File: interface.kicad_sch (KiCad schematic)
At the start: 2 parts, among them U1 2.42OLED

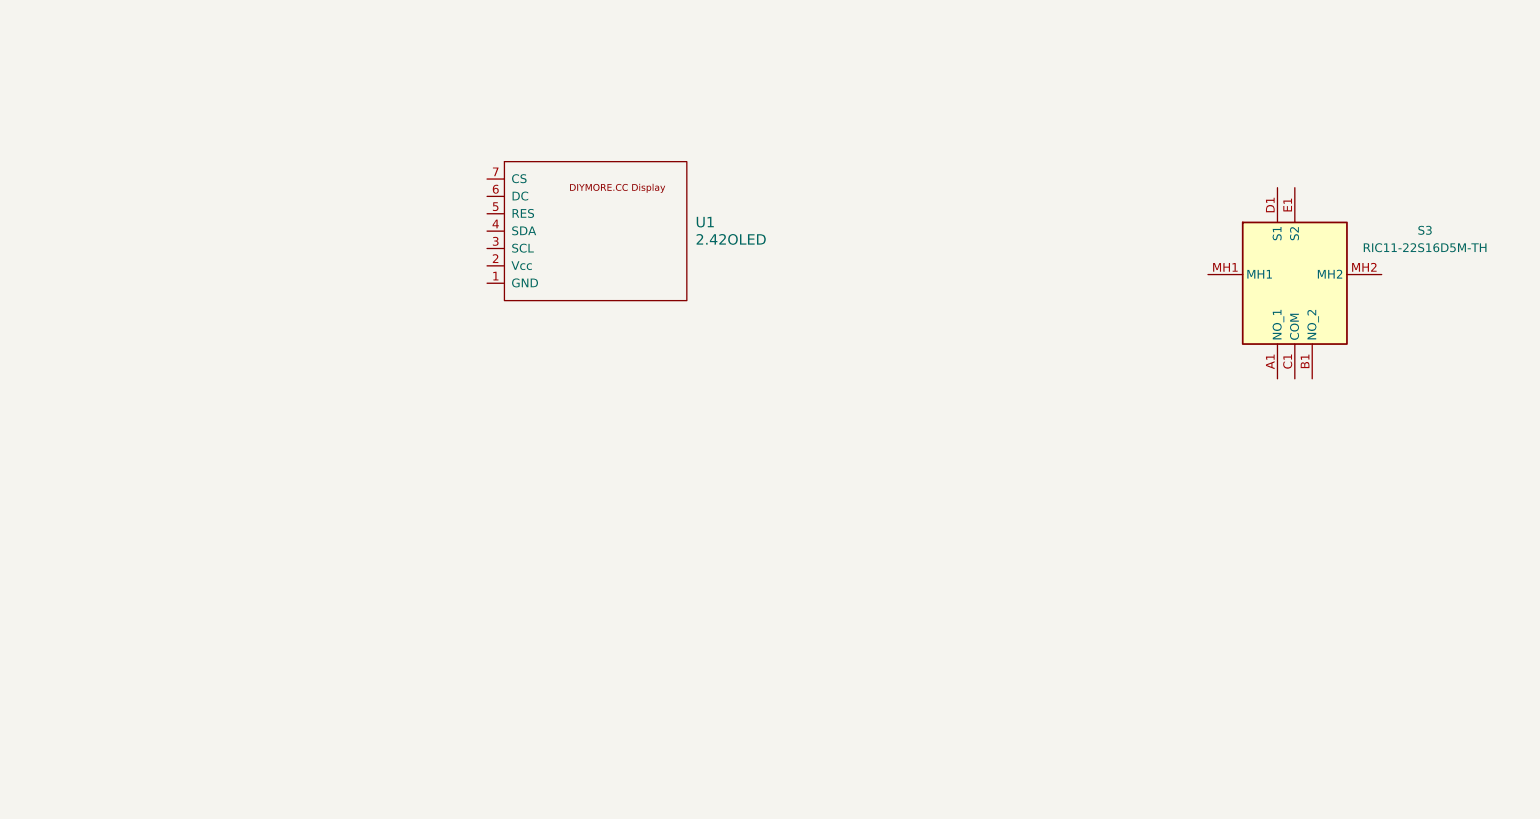
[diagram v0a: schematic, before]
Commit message: improve power delivery schema, improve dac, added oled, encoder, audio out
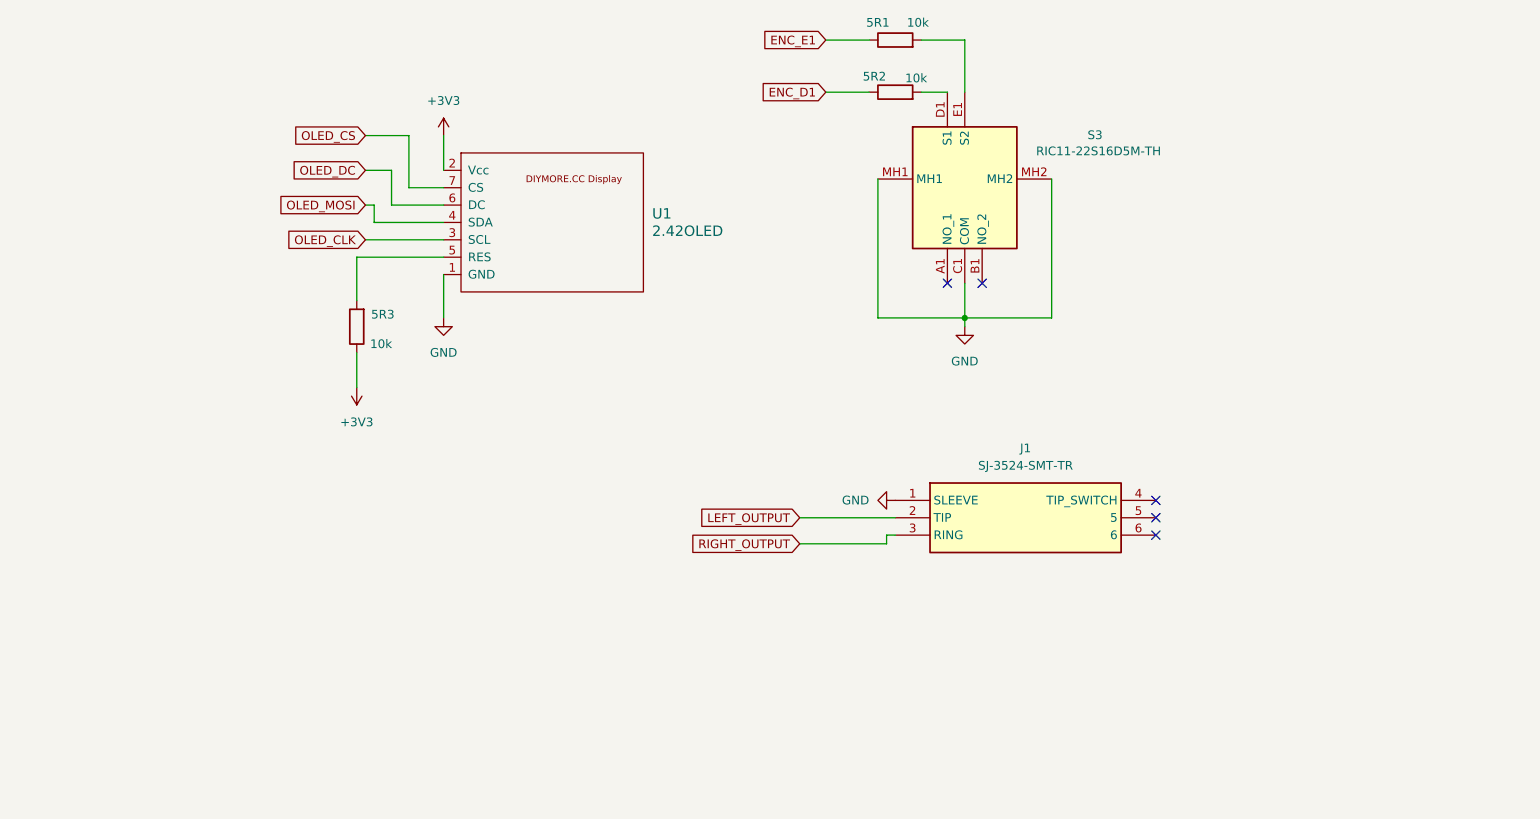
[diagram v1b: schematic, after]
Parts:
- added 5R1, 5R2, 5R3: 10k, symbol Device:R
- added J1: SJ-3524-SMT-TR, ipradio:SJ3524SMTTR, symbol ipradio:SJ-3524-SMT-TR
- S3: footprint RIC1122S16D5MTH -> ipradio:RIC1122S16D5MTH
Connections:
- net GND: now reaches U1.1 (GND)
- net GND: now also S3.C1 (COM), S3.MH1, S3.MH2, J1.1 (SLEEVE)
- net +3V3: now reaches U1.2 (Vcc)
- net +3V3: now also 5R3.1
- net OLED_CLK: now reaches U1.3 (SCL)
- net OLED_MOSI: now reaches U1.4 (SDA)
- net at U1.5 (RES): now also 5R3.2
- net OLED_DC: now reaches U1.6 (DC)
- net OLED_CS: now reaches U1.7 (CS)
- net at S3.D1 (S1): now also 5R2.2
- net at S3.E1 (S2): now also 5R1.2
- new net ENC_D1: 5R2.1
- new net ENC_E1: 5R1.1
- new net LEFT_OUTPUT: J1.2 (TIP)
- new net RIGHT_OUTPUT: J1.3 (RING)
- no-connect marks 0 -> 5
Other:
- moved on the sheet: S3, U1

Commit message: finalize power and esp schemas
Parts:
- 5R1, 5R2, 5R3: footprint (none) -> Resistor_SMD:R_0402_1005Metric
- U1: footprint (none) -> ipradio:DIYMORE.CC
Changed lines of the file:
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@@
 	(paper "A4")
+	(junction
+		(at 100.33 62.23)
+		(diameter 0)
+		(color 0 0 0 0)
+	)
 	(junction
 		(at 176.53 88.9)
@@
 			)
 		)
-		(property "Footprint" ""
+		(property "Footprint" "Resistor_SMD:R_0402_1005Metric"
 			(at 166.37 57.658 90)
 			(hide yes)
@@
 			)
 		)
-		(property "Footprint" ""
+		(property "Footprint" "Resistor_SMD:R_0402_1005Metric"
 			(at 166.37 50.038 90)
 			(hide yes)
@@
 			)
 		)
-		(property "Footprint" ""
+		(property "Footprint" "ipradio:DIYMORE.CC"
 			(at 102.87 86.36 0)
 			(hide yes)
@@
 			)
 		)
-		(property "Footprint" ""
+		(property "Footprint" "Resistor_SMD:R_0402_1005Metric"
 			(at 89.408 90.17 90)
 			(hide yes)
@@
 					(unit 1)
 				)
+			)
+		)
+	)
+	(symbol
+		(lib_id "power:PWR_FLAG")
+		(at 100.33 62.23 270)
+		(unit 1)
+		(body_style 1)
+		(exclude_from_sim no)
+		(in_bom yes)
+		(on_board yes)
+		(in_pos_files yes)
+		(dnp no)
+		(fields_autoplaced yes)
+		(property "Reference" "#FLG01"
+			(at 102.235 62.23 0)
+			(hide yes)
+			(show_name no)
+			(do_not_autoplace no)
+			(effects
+				(font
+					(size 1.27 1.27)
+				)
+			)
+		)
+		(property "Value" "PWR_FLAG"
+			(at 104.14 62.2299 90)
+			(show_name no)
+			(do_not_autoplace no)
+			(effects
+				(font
+					(size 1.27 1.27)
+				)
+				(justify left)
+			)
+		)
+		(property "Footprint" ""
+			(at 100.33 62.23 0)
+			(hide yes)
+			(show_name no)
+			(do_not_autoplace no)
+			(effects
+				(font
+					(size 1.27 1.27)
+				)
+			)
+		)
+		(property "Datasheet" ""
+			(at 100.33 62.23 0)
+			(hide yes)
+			(show_name no)
+			(do_not_autoplace no)
+			(effects
+				(font
+					(size 1.27 1.27)
+				)
+			)
+		)
+		(property "Description" "Special symbol for telling ERC where power comes from"
+			(at 100.33 62.23 0)
+			(hide yes)
+			(show_name no)
+			(do_not_autoplace no)
+			(effects
+				(font
+					(size 1.27 1.27)
+				)
+			)
+		)
+		(pin "1"
+		)
+		(instances
+			(project "ipradio"
+				(path "/8a54d64b-fc0c-416f-bc23-c8cdbd245f9f/68655846-d262-4627-826b-c40a0dd3f1c4"
+					(reference "#FLG01")
+					(unit 1)
+				)

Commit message: finalized schema
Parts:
- added 5C3, 5C4, 5C7: 100nF, Capacitor_SMD:C_0402_1005Metric, symbol Device:C
- added 5C5: 1uF, Capacitor_SMD:C_0402_1005Metric, symbol Device:C
- added 5C6: 10uF, Capacitor_SMD:C_0402_1005Metric, symbol Device:C
- added R2, R3, R4: 5.1k, Resistor_SMD:R_0402_1005Metric, symbol Device:R
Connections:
- net ENC_D1 is gone; now on net +3V3: 5R2.1
- net ENC_E1 is gone; now on net +3V3: 5R1.1
- net +3V3: now also 5R3.2, 5C4.2, 5C5.2, 5C6.2, 5C7.1, R2.1, R3.1, R4.1; no longer 5R3.1
- net GND: now also 5C3.2, 5C4.1, 5C5.1, 5C6.1, 5C7.2; no longer J1.1 (SLEEVE)
- net ENC_DT: now reaches 5R2.2
- net ENC_DT: now also S3.A1 (NO_1); no longer S3.D1 (S1)
- net ENC_CLK: now reaches 5R1.2
- net ENC_CLK: now also S3.B1 (NO_2); no longer S3.E1 (S2)
- net at U1.5 (RES): now also 5R3.1; no longer 5R3.2
- net OLED_CLK renamed I2S_CLK
- net I2S_CLK: now also R2.2
- net OLED_CS: no longer names the net of U1.7 (CS)
- net OLED_DC: no longer names the net of U1.6 (DC)
- net OLED_MOSI renamed I2S_SDA
- net I2S_SDA: now also R3.2
- new net ENC_SW: 5C3.1, R4.2, S3.D1 (S1), S3.E1 (S2)
- new net GNDA: J1.1 (SLEEVE)
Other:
- moved on the sheet: 5R1, 5R2, 5R3, J1, S3, U1
